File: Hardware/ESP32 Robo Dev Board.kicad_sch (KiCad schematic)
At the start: 18 parts, among them J1 PRG, U1 ESP32-S3-WROOM-1, U2 AMS1117-3.3

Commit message: Fixup! Better anotations
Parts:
- J_B2: renamed from J_B1; value (none) -> Batt In; footprint (none) -> Connector_JST:JST_EH_B2B-EH-A_1x02_P2.50mm_Vertical
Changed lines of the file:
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@@
   (symbol (lib_id "power:GND") (at 207.01 48.26 0) (unit 1)
     (in_bom yes) (on_board yes) (fields_autoplaced)
-    (property "Reference" "#PWR07" (id 0) (at 207.01 54.61 0)
+    (property "Reference" "#PWR08" (id 0) (at 207.01 54.61 0)
       (effects (font (size 1.27 1.27)) hide)
     )
@@
   (symbol (lib_id "power:GND") (at 205.74 26.67 0) (unit 1)
     (in_bom yes) (on_board yes)
-    (property "Reference" "#PWR?" (id 0) (at 205.74 33.02 0)
+    (property "Reference" "#PWR07" (id 0) (at 205.74 33.02 0)
       (effects (font (size 1.27 1.27)) hide)
     )
@@
   (symbol (lib_id "Connector:Conn_01x02_Male") (at 199.39 22.86 0) (unit 1)
     (in_bom yes) (on_board yes)
-    (property "Reference" "J_B1" (id 0) (at 203.2 20.32 0)
-      (effects (font (size 1.27 1.27)) (justify right))
-    )
-    (property "Value" "" (id 1) (at 204.47 17.78 0)
-      (effects (font (size 1.27 1.27)) (justify right))
-    )
-    (property "Footprint" "" (id 2) (at 199.39 22.86 0)
+    (property "Reference" "J_B2" (id 0) (at 203.2 20.32 0)
+      (effects (font (size 1.27 1.27)) (justify right))
+    )
+    (property "Value" "Batt In" (id 1) (at 204.47 17.78 0)
+      (effects (font (size 1.27 1.27)) (justify right))
+    )
+    (property "Footprint" "Connector_JST:JST_EH_B2B-EH-A_1x02_P2.50mm_Vertical" (id 2) (at 199.39 22.86 0)
       (effects (font (size 1.27 1.27)) hide)
     )
@@
       (reference "#PWR06") (unit 1) (value "GND") (footprint "")
     )
+    (path "/763b259e-f9f8-4217-9efd-65ca784f6851"
+      (reference "#PWR07") (unit 1) (value "GND") (footprint "")
+    )
     (path "/713083df-12bf-4081-9211-169792f90f86"
-      (reference "#PWR07") (unit 1) (value "GND") (footprint "")
+      (reference "#PWR08") (unit 1) (value "GND") (footprint "")
     )
     (path "/2a967591-2c10-4303-bb18-7a855e4ea57c"
@@
       (reference "#PWR044") (unit 1) (value "GND") (footprint "")
     )
-    (path "/763b259e-f9f8-4217-9efd-65ca784f6851"
-      (reference "#PWR?") (unit 1) (value "GND") (footprint "")
-    )
     (path "/8f68081f-33f7-4342-b1f0-d2938b6c2bf0"
       (reference "C1") (unit 1) (value "2.2 µF") (footprint "Capacitor_SMD:C_0805_2012Metric")
@@
     )
     (path "/a3149699-8a34-42d1-ac77-5fe843d39d26"
-      (reference "J_B1") (unit 1) (value "Batt In") (footprint "Connector_JST:JST_EH_B2B-EH-A_1x02_P2.50mm_Vertical")
+      (reference "J_B2") (unit 1) (value "Batt In") (footprint "Connector_JST:JST_EH_B2B-EH-A_1x02_P2.50mm_Vertical")
     )
     (path "/b9644345-2c8d-4f54-9d32-2353cd6b3881"

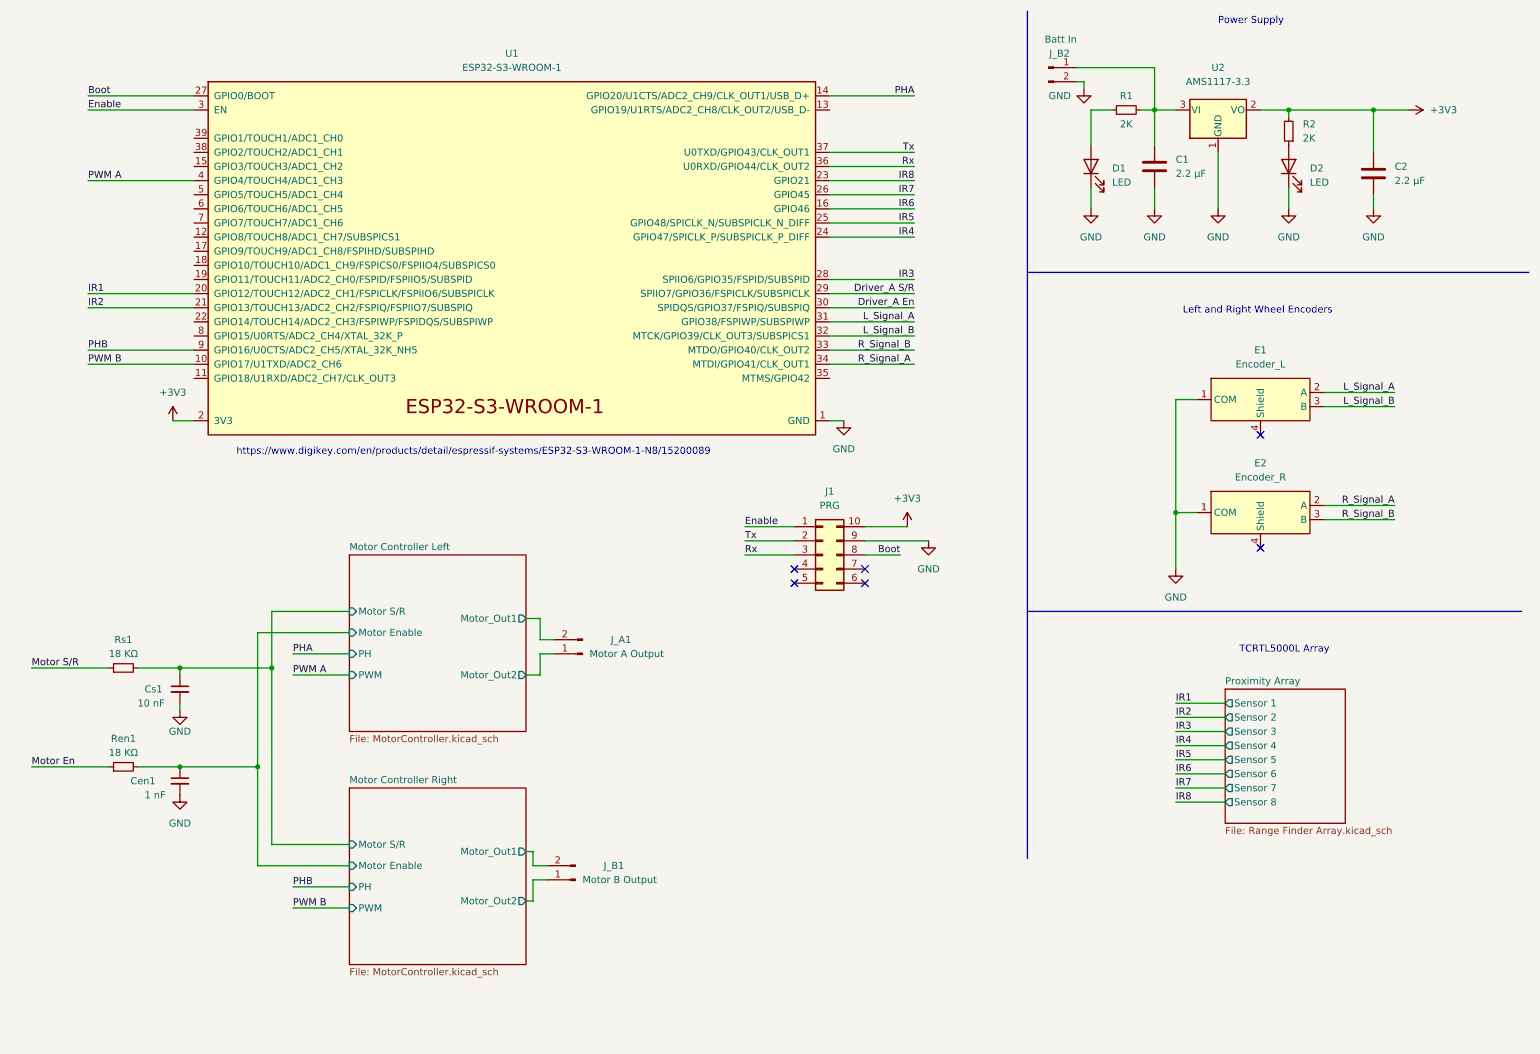
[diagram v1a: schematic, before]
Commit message: Rebuild Layout
Took the V1.0 Layout and reworked it.
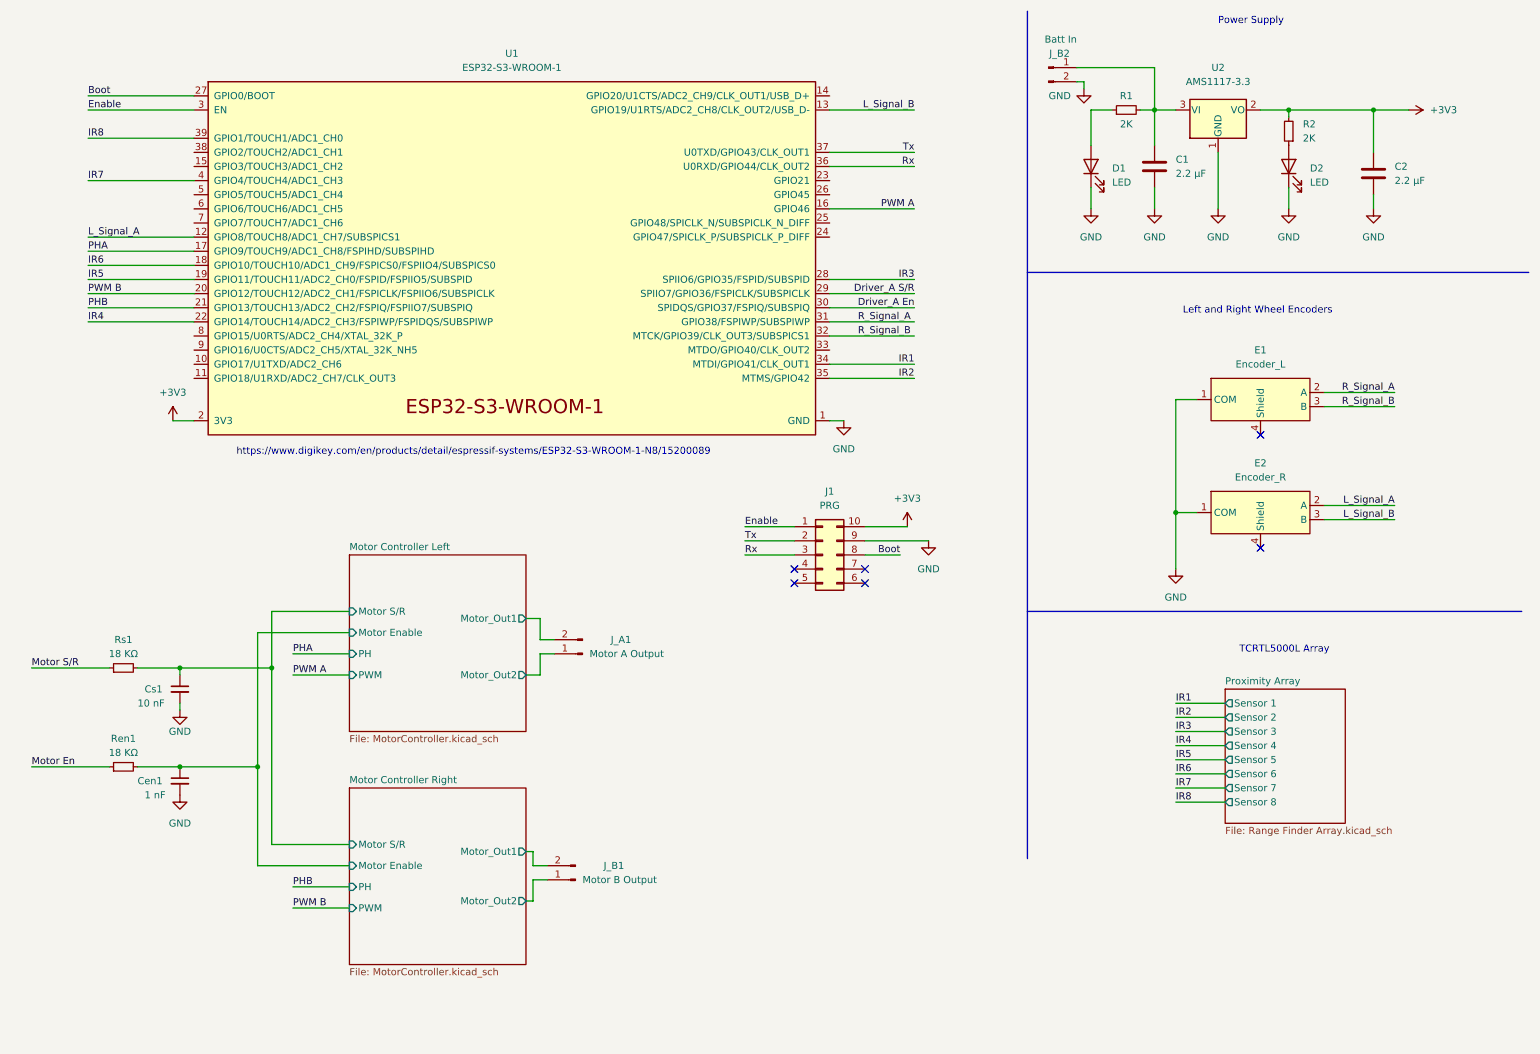
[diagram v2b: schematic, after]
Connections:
- net IR1: now also U1.34 (MTDI/GPIO41/CLK_OUT1); no longer U1.20 (GPIO12/TOUCH12/ADC2_CH1/FSPICLK/FSPIIO6/SUBSPICLK)
- net IR2: now also U1.35 (MTMS/GPIO42); no longer U1.21 (GPIO13/TOUCH13/ADC2_CH2/FSPIQ/FSPIIO7/SUBSPIQ)
- net IR4: now also U1.22 (GPIO14/TOUCH14/ADC2_CH3/FSPIWP/FSPIDQS/SUBSPIWP); no longer U1.24 (GPIO47/SPICLK_P/SUBSPICLK_P_DIFF)
- net IR5: now also U1.19 (GPIO11/TOUCH11/ADC2_CH0/FSPID/FSPIIO5/SUBSPID); no longer U1.25 (GPIO48/SPICLK_N/SUBSPICLK_N_DIFF)
- net IR6: now also U1.18 (GPIO10/TOUCH10/ADC1_CH9/FSPICS0/FSPIIO4/SUBSPICS0); no longer U1.16 (GPIO46)
- net IR7: now also U1.4 (GPIO4/TOUCH4/ADC1_CH3); no longer U1.26 (GPIO45)
- net IR8: now also U1.39 (GPIO1/TOUCH1/ADC1_CH0); no longer U1.23 (GPIO21)
- net L_Signal_A: now also E2.2 (A), U1.12 (GPIO8/TOUCH8/ADC1_CH7/SUBSPICS1); no longer E1.2 (A), U1.31 (GPIO38/FSPIWP/SUBSPIWP)
- net L_Signal_B: now also E2.3 (B), U1.13 (GPIO19/U1RTS/ADC2_CH8/CLK_OUT2/USB_D-); no longer E1.3 (B), U1.32 (MTCK/GPIO39/CLK_OUT3/SUBSPICS1)
- net PHA: now also U1.17 (GPIO9/TOUCH9/ADC1_CH8/FSPIHD/SUBSPIHD); no longer U1.14 (GPIO20/U1CTS/ADC2_CH9/CLK_OUT1/USB_D+)
- net PHB: now also U1.21 (GPIO13/TOUCH13/ADC2_CH2/FSPIQ/FSPIIO7/SUBSPIQ); no longer U1.9 (GPIO16/U0CTS/ADC2_CH5/XTAL_32K_NH5)
- net PWM A: now also U1.16 (GPIO46); no longer U1.4 (GPIO4/TOUCH4/ADC1_CH3)
- net PWM B: now also U1.20 (GPIO12/TOUCH12/ADC2_CH1/FSPICLK/FSPIIO6/SUBSPICLK); no longer U1.10 (GPIO17/U1TXD/ADC2_CH6)
- net R_Signal_A: now also E1.2 (A), U1.31 (GPIO38/FSPIWP/SUBSPIWP); no longer E2.2 (A), U1.34 (MTDI/GPIO41/CLK_OUT1)
- net R_Signal_B: now also E1.3 (B), U1.32 (MTCK/GPIO39/CLK_OUT3/SUBSPICS1); no longer E2.3 (B), U1.33 (MTDO/GPIO40/CLK_OUT2)

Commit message: Update ESP32 Robo Dev Board.kicad_sch
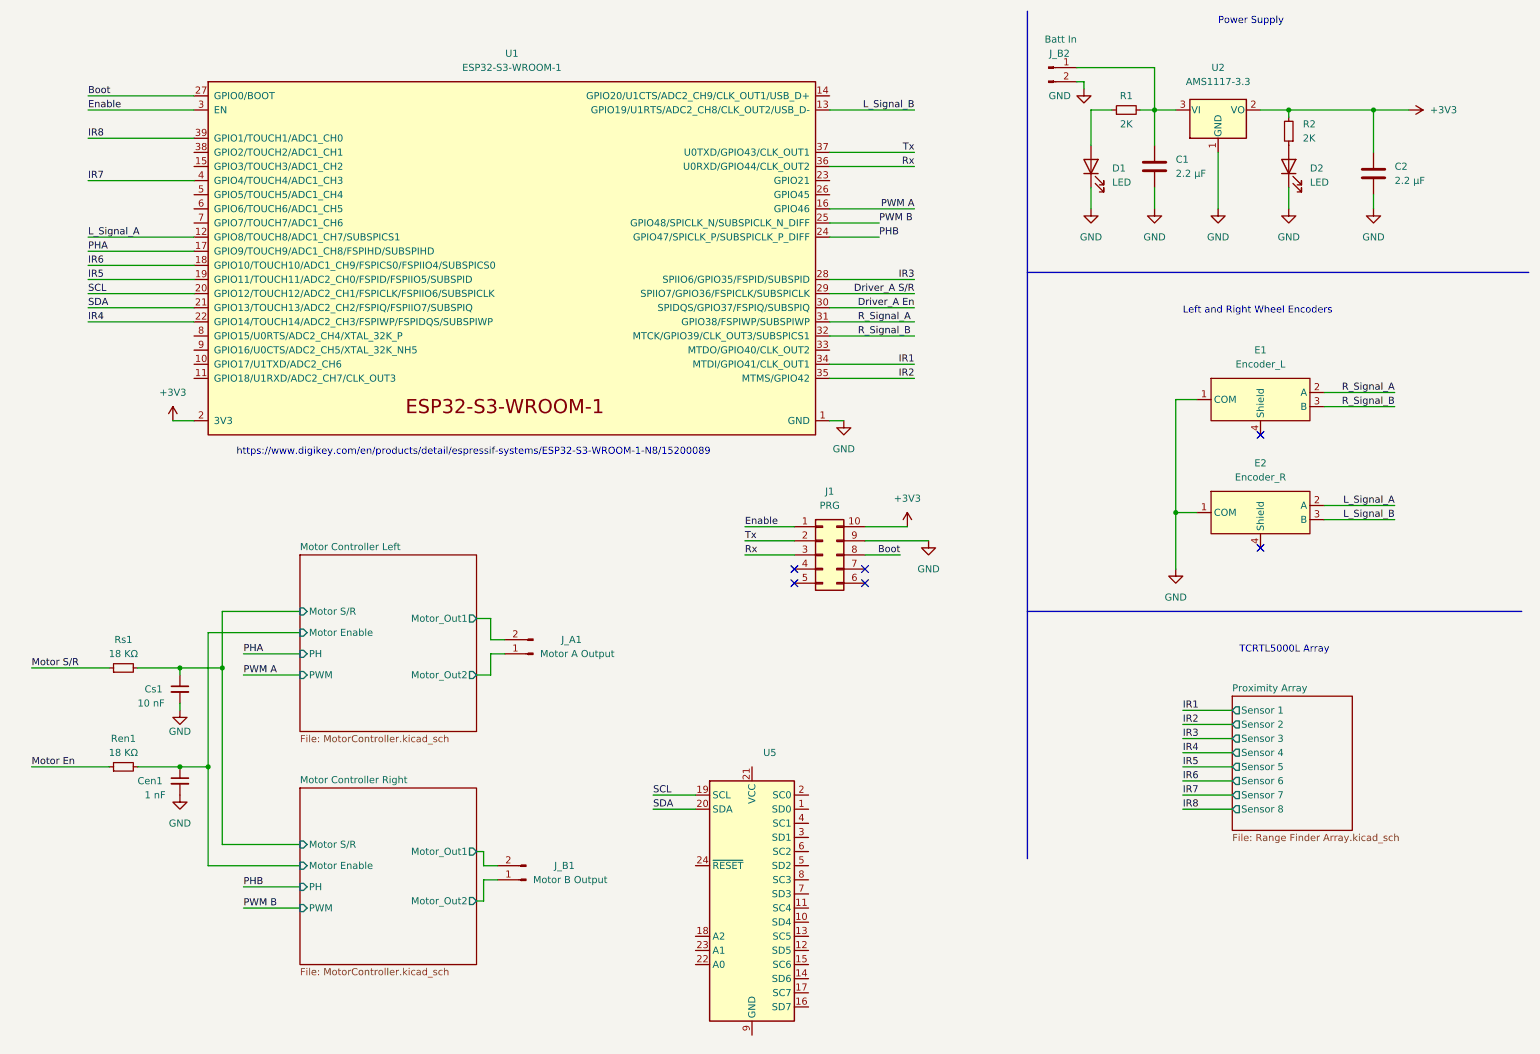
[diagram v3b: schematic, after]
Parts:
- added U5: (no value), symbol Interface_Expansion:TCA9548ARGER
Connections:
- net PHB: now also U1.24 (GPIO47/SPICLK_P/SUBSPICLK_P_DIFF); no longer U1.21 (GPIO13/TOUCH13/ADC2_CH2/FSPIQ/FSPIIO7/SUBSPIQ)
- net PWM B: now also U1.25 (GPIO48/SPICLK_N/SUBSPICLK_N_DIFF); no longer U1.20 (GPIO12/TOUCH12/ADC2_CH1/FSPICLK/FSPIIO6/SUBSPICLK)
- new net SCL: U1.20 (GPIO12/TOUCH12/ADC2_CH1/FSPICLK/FSPIIO6/SUBSPICLK), U5.19 (SCL)
- new net SDA: U1.21 (GPIO13/TOUCH13/ADC2_CH2/FSPIQ/FSPIIO7/SUBSPIQ), U5.20 (SDA)
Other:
- moved on the sheet: J_A1, J_B1

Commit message: Add new array for sensors
Add in sensor array

Begin trace reroute
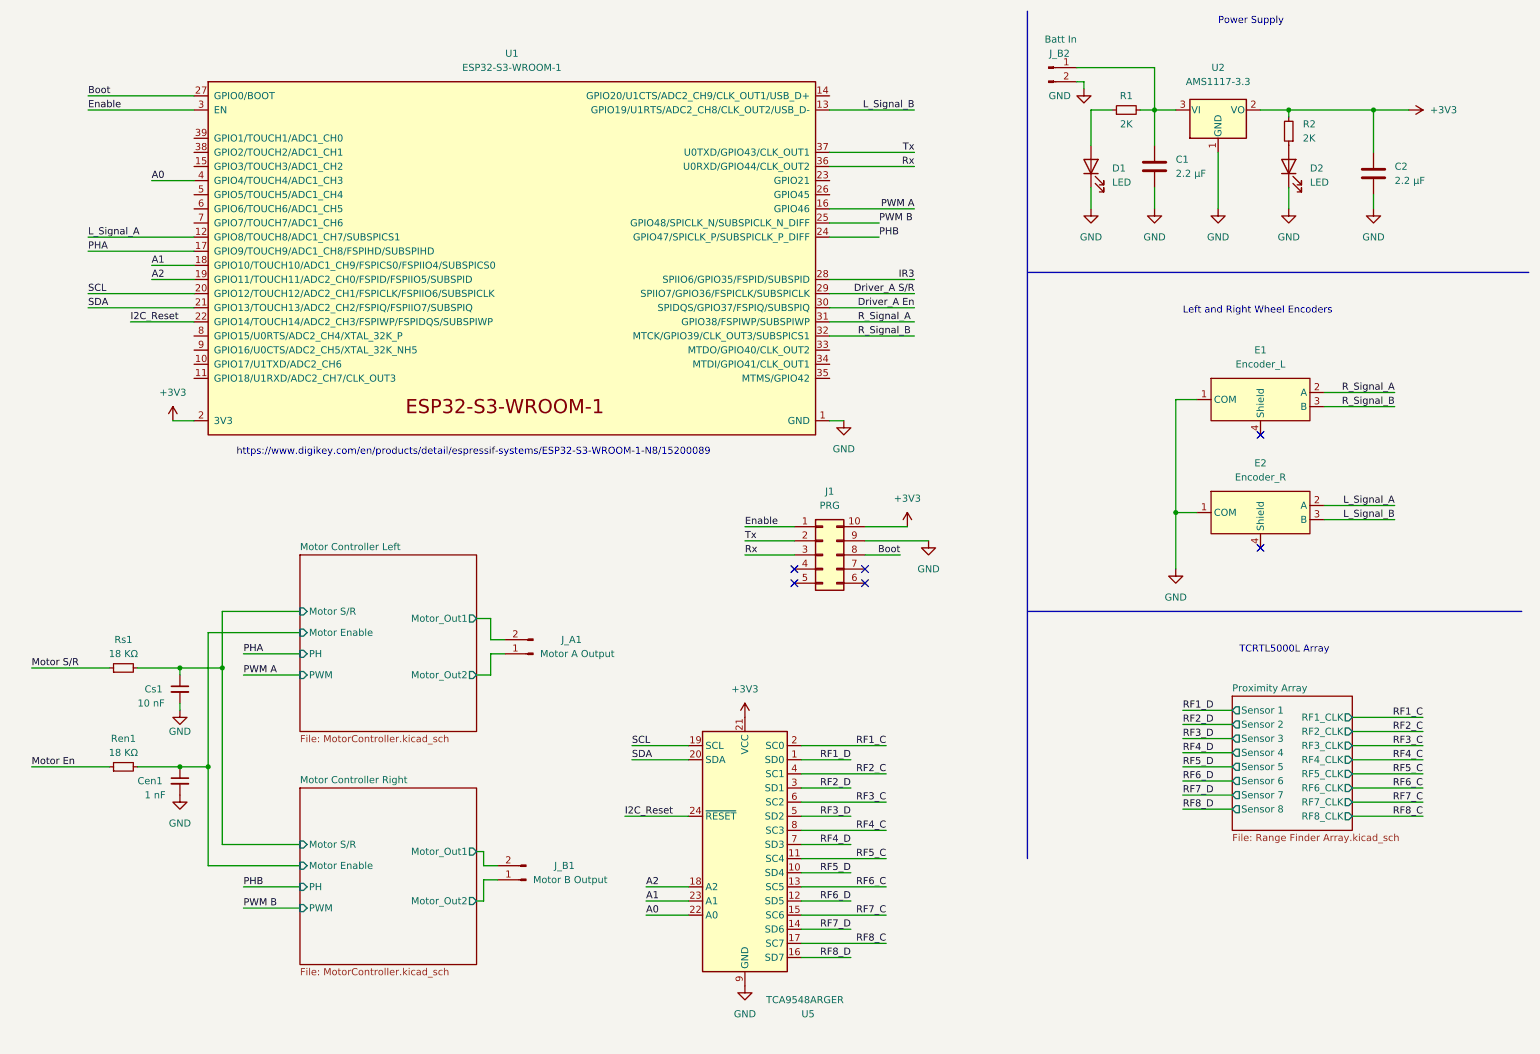
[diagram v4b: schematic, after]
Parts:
- U5: value (none) -> TCA9548ARGER; footprint (none) -> Package_DFN_QFN:Texas_RGE0024C_EP2.1x2.1mm
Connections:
- net IR4 is gone; now on net I2C_Reset: U1.22 (GPIO14/TOUCH14/ADC2_CH3/FSPIWP/FSPIDQS/SUBSPIWP)
- net IR5 is gone; now on net A2: U1.19 (GPIO11/TOUCH11/ADC2_CH0/FSPID/FSPIIO5/SUBSPID)
- net IR6 is gone; now on net A1: U1.18 (GPIO10/TOUCH10/ADC1_CH9/FSPICS0/FSPIIO4/SUBSPICS0)
- net IR7 is gone; now on net A0: U1.4 (GPIO4/TOUCH4/ADC1_CH3)
- net +3V3: now also U5.21 (VCC)
- net GND: now also U5.9 (GND)
- net RF1_D: now reaches U5.1 (SD0)
- net RF5_D: now reaches U5.10 (SD4)
- net RF5_C: now reaches U5.11 (SC4)
- net RF6_D: now reaches U5.12 (SD5)
- net RF6_C: now reaches U5.13 (SC5)
- net RF7_D: now reaches U5.14 (SD6)
- net RF7_C: now reaches U5.15 (SC6)
- net RF8_D: now reaches U5.16 (SD7)
- net RF8_C: now reaches U5.17 (SC7)
- net A2: now reaches U5.18 (A2)
- net RF1_C: now reaches U5.2 (SC0)
- net A0: now reaches U5.22 (A0)
- net A1: now reaches U5.23 (A1)
- net I2C_Reset: now reaches U5.24 (~{RESET})
- net RF2_D: now reaches U5.3 (SD1)
- net RF2_C: now reaches U5.4 (SC1)
- net RF3_D: now reaches U5.5 (SD2)
- net RF3_C: now reaches U5.6 (SC2)
- net RF4_D: now reaches U5.7 (SD3)
- net RF4_C: now reaches U5.8 (SC3)
- net IR1: no longer names the net of U1.34 (MTDI/GPIO41/CLK_OUT1)
- net IR2: no longer names the net of U1.35 (MTMS/GPIO42)
- net IR8: no longer names the net of U1.39 (GPIO1/TOUCH1/ADC1_CH0)
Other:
- sheet Proximity Array ports: added RF1_CLK, RF2_CLK, RF3_CLK, RF4_CLK, RF5_CLK, RF6_CLK, RF7_CLK, RF8_CLK; removed none
- moved on the sheet: U5
